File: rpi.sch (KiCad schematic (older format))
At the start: 8 parts, among them J1 Power Connector, P1 RPi-Header

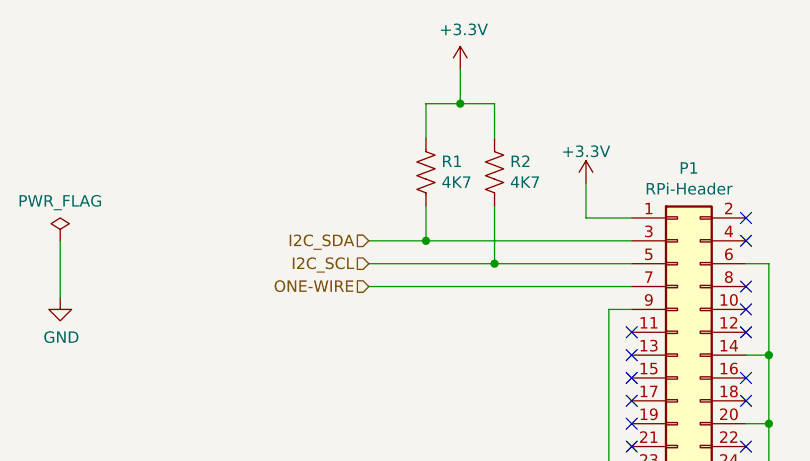
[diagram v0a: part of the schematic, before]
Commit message: Added MFN, MPN, VN and VPN fields for all symbols
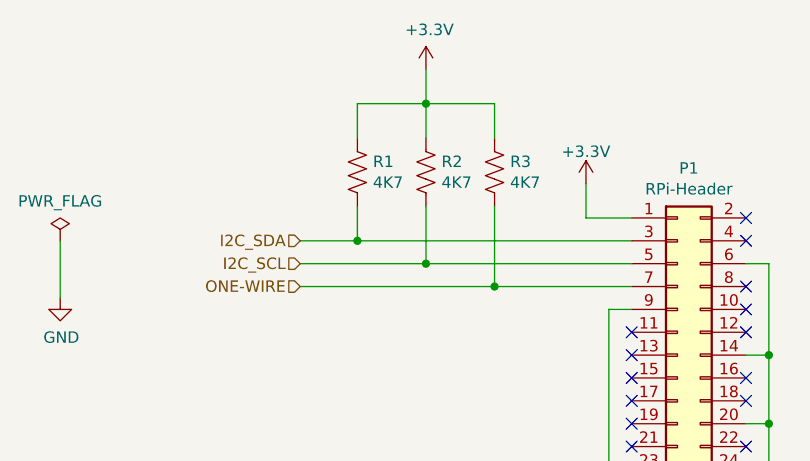
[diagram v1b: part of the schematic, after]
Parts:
- added R3: 4K7, Resistor_SMD:R_0603_1608Metric_Pad1.05x0.95mm_HandSolder, symbol Device:R_US
- J1: MFN (none) -> CUI Devices; MPN (none) -> TBP02R1-381-03BE; VN (none) -> Digikey; VPN (none) -> 102-6481-ND
- MK1, MK2, MK3, MK4: MFN (none) -> None; MPN (none) -> None; VN (none) -> None; VPN (none) -> None
- P1: MFN (none) -> Adafruit Industries LLC; MPN (none) -> 1979; VN (none) -> Digikey; VPN (none) -> 1528-1783-ND
- R1, R2: MFN (none) -> Generic; MPN (none) -> Generic; VN (none) -> Digikey; VPN (none) -> P4.7KDBCT-ND
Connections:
- net +3V3: now also R3.1
- net ONE-WIRE: now also R3.2
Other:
- moved on the sheet: R1, R2
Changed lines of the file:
@@
 F 1 "M2.5" H 6900 5355 50  0000 L CNN
 F 2 "MountingHole:MountingHole_2.7mm_M2.5" H 6800 5400 60  0001 C CNN
-F 3 "" H 6800 5400 60  0001 C CNN
+F 3 "~" H 6800 5400 60  0001 C CNN
+F 4 "None" H 6800 5400 50  0001 C CNN "VN"
+F 5 "None" H 6800 5400 50  0001 C CNN "MFN"
+F 6 "None" H 6800 5400 50  0001 C CNN "MPN"
+F 7 "None" H 6800 5400 50  0001 C CNN "VPN"
 	1    6800 5400
 	1    0    0    -1
@@
 F 1 "M2.5" H 7900 5355 50  0000 L CNN
 F 2 "MountingHole:MountingHole_2.7mm_M2.5" H 7800 5400 60  0001 C CNN
-F 3 "" H 7800 5400 60  0001 C CNN
+F 3 "~" H 7800 5400 60  0001 C CNN
+F 4 "None" H 7800 5400 50  0001 C CNN "VN"
+F 5 "None" H 7800 5400 50  0001 C CNN "MFN"
+F 6 "None" H 7800 5400 50  0001 C CNN "MPN"
+F 7 "None" H 7800 5400 50  0001 C CNN "VPN"
 	1    7800 5400
 	1    0    0    -1
@@
 F 1 "M2.5" H 7400 5355 50  0000 L CNN
 F 2 "MountingHole:MountingHole_2.7mm_M2.5" H 7300 5400 60  0001 C CNN
-F 3 "" H 7300 5400 60  0001 C CNN
+F 3 "~" H 7300 5400 60  0001 C CNN
+F 4 "None" H 7300 5400 50  0001 C CNN "VN"
+F 5 "None" H 7300 5400 50  0001 C CNN "MFN"
+F 6 "None" H 7300 5400 50  0001 C CNN "MPN"
+F 7 "None" H 7300 5400 50  0001 C CNN "VPN"
 	1    7300 5400
 	1    0    0    -1
@@
 F 1 "M2.5" H 8400 5355 50  0000 L CNN
 F 2 "MountingHole:MountingHole_2.7mm_M2.5" H 8300 5400 60  0001 C CNN
-F 3 "" H 8300 5400 60  0001 C CNN
+F 3 "~" H 8300 5400 60  0001 C CNN
+F 4 "None" H 8300 5400 50  0001 C CNN "VN"
+F 5 "None" H 8300 5400 50  0001 C CNN "MFN"
+F 6 "None" H 8300 5400 50  0001 C CNN "MPN"
+F 7 "None" H 8300 5400 50  0001 C CNN "VPN"
 	1    8300 5400
 	1    0    0    -1
@@
 Wire Wire Line
 	7950 3050 7850 3050
-Wire Wire Line
-	6200 3150 7350 3150
-Wire Wire Line
-	6200 3050 6750 3050
-Wire Wire Line
-	7350 2950 6450 2950
 Connection ~ 7250 4050
 Wire Wire Line
@@
 F 1 "RPi-Header" H 7600 4776 50  0000 C CNN
 F 2 "Connector_PinSocket_2.54mm:PinSocket_2x20_P2.54mm_Vertical" H 2700 2800 50  0001 C CNN
-F 3 "" H 2700 2800 50  0001 C CNN
+F 3 "https://media.digikey.com/pdf/Data%20Sheets/Adafruit%20PDFs/1979_Web.pdf" H 2700 2800 50  0001 C CNN
+F 4 "Adafruit Industries LLC" H 7550 3750 50  0001 C CNN "MFN"
+F 5 "1979" H 7550 3750 50  0001 C CNN "MPN"
+F 6 "Digikey" H 7550 3750 50  0001 C CNN "VN"
+F 7 "1528-1783-ND" H 7550 3750 50  0001 C CNN "VPN"
 	1    7550 3750
 	1    0    0    -1
@@
 NoConn ~ 7350 3650
 NoConn ~ 7350 4250
-Text HLabel 6200 2950 0    50   Input ~ 0
+Text HLabel 5900 2950 0    50   Input ~ 0
 I2C_SDA
-Text HLabel 6200 3050 0    50   Input ~ 0
+Text HLabel 5900 3050 0    50   Input ~ 0
 I2C_SCL
-Text HLabel 6200 3150 0    50   Input ~ 0
+Text HLabel 5900 3150 0    50   Input ~ 0
 ONE-WIRE
 $Comp
@@
 F 1 "Power Connector" H 3768 3766 50  0000 C CNN
 F 2 "Connector_Phoenix_MC:PhoenixContact_MC_1,5_3-G-3.81_1x03_P3.81mm_Horizontal" H 3850 4000 50  0001 C CNN
-F 3 "~" H 3850 4000 50  0001 C CNN
+F 3 "https://www.cuidevices.com/product/resource/tbp02r1-381.pdf" H 3850 4000 50  0001 C CNN
+F 4 "Digikey" H 3850 4000 50  0001 C CNN "VN"
+F 5 "CUI Devices" H 3850 4000 50  0001 C CNN "MFN"
+F 6 "TBP02R1-381-03BE" H 3850 4000 50  0001 C CNN "MPN"
+F 7 "102-6481-ND" H 3850 4000 50  0001 C CNN "VPN"
 	1    3850 4000
 	-1   0    0    1
@@
 L Device:R_US R?
 U 1 1 5E5D64A6
-P 6450 2650
+P 6150 2650
 AR Path="/5E5D64A6" Ref="R?"  Part="1"
 AR Path="/5E624F1D/5E5D64A6" Ref="R?"  Part="1"
 AR Path="/5E49EFD8/5E5D64A6" Ref="R1"  Part="1"
-F 0 "R1" H 6518 2696 50  0000 L CNN
+F 0 "R1" H 6218 2696 50  0000 L CNN
+F 1 "4K7" H 6218 2605 50  0000 L CNN
+F 2 "Resistor_SMD:R_0603_1608Metric_Pad1.05x0.95mm_HandSolder" V 6190 2640 50  0001 C CNN
+F 3 "~" H 6150 2650 50  0001 C CNN
+F 4 "Digikey" H 6150 2650 50  0001 C CNN "VN"
+F 5 "Generic" H 6150 2650 50  0001 C CNN "MFN"
+F 6 "Generic" H 6150 2650 50  0001 C CNN "MPN"
+F 7 "P4.7KDBCT-ND" H 6150 2650 50  0001 C CNN "VPN"
+	1    6150 2650
+	1    0    0    -1
+$EndComp
+$Comp
+L power:+3.3V #PWR?
+U 1 1 5E5D64AD
+P 6450 2200
+AR Path="/5E5D64AD" Ref="#PWR?"  Part="1"
+AR Path="/5E624F1D/5E5D64AD" Ref="#PWR?"  Part="1"
+AR Path="/5E49EFD8/5E5D64AD" Ref="#PWR0139"  Part="1"
+F 0 "#PWR0139" H 6450 2050 50  0001 C CNN
+F 1 "+3.3V" H 6465 2373 50  0000 C CNN
+F 2 "" H 6450 2200 50  0001 C CNN
+F 3 "" H 6450 2200 50  0001 C CNN
+	1    6450 2200
+	1    0    0    -1
+$EndComp
+Wire Wire Line
+	6750 2350 6750 2500
+$Comp
+L Device:R_US R?
+U 1 1 5E5D64B5
+P 6450 2650
+AR Path="/5E5D64B5" Ref="R?"  Part="1"
+AR Path="/5E624F1D/5E5D64B5" Ref="R?"  Part="1"
+AR Path="/5E49EFD8/5E5D64B5" Ref="R2"  Part="1"
+F 0 "R2" H 6518 2696 50  0000 L CNN
 F 1 "4K7" H 6518 2605 50  0000 L CNN
 F 2 "Resistor_SMD:R_0603_1608Metric_Pad1.05x0.95mm_HandSolder" V 6490 2640 50  0001 C CNN
 F 3 "~" H 6450 2650 50  0001 C CNN
+F 4 "Digikey" H 6450 2650 50  0001 C CNN "VN"
+F 5 "Generic" H 6450 2650 50  0001 C CNN "MFN"
+F 6 "Generic" H 6450 2650 50  0001 C CNN "MPN"
+F 7 "P4.7KDBCT-ND" H 6450 2650 50  0001 C CNN "VPN"
 	1    6450 2650
 	1    0    0    -1
 $EndComp
-$Comp
-L power:+3.3V #PWR?
-U 1 1 5E5D64AD
-P 6600 2200
-AR Path="/5E5D64AD" Ref="#PWR?"  Part="1"
-AR Path="/5E624F1D/5E5D64AD" Ref="#PWR?"  Part="1"
-AR Path="/5E49EFD8/5E5D64AD" Ref="#PWR0139"  Part="1"
-F 0 "#PWR0139" H 6600 2050 50  0001 C CNN
-F 1 "+3.3V" H 6615 2373 50  0000 C CNN
-F 2 "" H 6600 2200 50  0001 C CNN
-F 3 "" H 6600 2200 50  0001 C CNN
-	1    6600 2200
-	1    0    0    -1
-$EndComp
-Wire Wire Line
-	6750 2350 6750 2500
-$Comp
-L Device:R_US R?
-U 1 1 5E5D64B5
-P 6750 2650
-AR Path="/5E5D64B5" Ref="R?"  Part="1"
-AR Path="/5E624F1D/5E5D64B5" Ref="R?"  Part="1"
-AR Path="/5E49EFD8/5E5D64B5" Ref="R2"  Part="1"
-F 0 "R2" H 6818 2696 50  0000 L CNN
-F 1 "4K7" H 6818 2605 50  0000 L CNN
-F 2 "Resistor_SMD:R_0603_1608Metric_Pad1.05x0.95mm_HandSolder" V 6790 2640 50  0001 C CNN
-F 3 "~" H 6750 2650 50  0001 C CNN
-	1    6750 2650
-	1    0    0    -1
-$EndComp
-Wire Wire Line
-	6450 2350 6600 2350
-Wire Wire Line
-	6600 2200 6600 2350
-Connection ~ 6600 2350
-Wire Wire Line
-	6600 2350 6750 2350
+Wire Wire Line
+	6450 2200 6450 2350
 Wire Wire Line
 	6450 2500 6450 2350
 Wire Wire Line
-	6450 2800 6450 2950
-Connection ~ 6450 2950
-Wire Wire Line
-	6450 2950 6200 2950
-Wire Wire Line
-	6750 2800 6750 3050
-Connection ~ 6750 3050
-Wire Wire Line
-	6750 3050 7350 3050
+	6150 2950 5900 2950
 NoConn ~ 7850 3150
 NoConn ~ 7850 3250
@@
 Wire Wire Line
 	4850 2950 4850 3200
+$Comp
+L Device:R_US R?
+U 1 1 5E62CDA9
+P 6750 2650
+AR Path="/5E62CDA9" Ref="R?"  Part="1"
+AR Path="/5E64C909/5E62CDA9" Ref="R?"  Part="1"
+AR Path="/5E49EFD8/5E62CDA9" Ref="R3"  Part="1"
+F 0 "R3" H 6818 2696 50  0000 L CNN
+F 1 "4K7" H 6818 2605 50  0000 L CNN
+F 2 "Resistor_SMD:R_0603_1608Metric_Pad1.05x0.95mm_HandSolder" V 6790 2640 50  0001 C CNN
+F 3 "~" H 6750 2650 50  0001 C CNN
+F 4 "Digikey" H 6750 2650 50  0001 C CNN "VN"
+F 5 "Generic" H 6750 2650 50  0001 C CNN "MFN"
+F 6 "Generic" H 6750 2650 50  0001 C CNN "MPN"
+F 7 "P4.7KDBCT-ND" H 6750 2650 50  0001 C CNN "VPN"
+	1    6750 2650
+	1    0    0    -1
+$EndComp
+Wire Wire Line
+	6150 2350 6150 2500
+Wire Wire Line
+	6150 2350 6450 2350
+Connection ~ 6450 2350
+Wire Wire Line
+	6450 2350 6750 2350
+Wire Wire Line
+	6150 2800 6150 2950
+Wire Wire Line
+	6150 2950 7350 2950
+Connection ~ 6150 2950
+Wire Wire Line
+	5900 3050 6450 3050
+Wire Wire Line
+	5900 3150 6750 3150
+Wire Wire Line
+	6450 2800 6450 3050
+Connection ~ 6450 3050
+Wire Wire Line
+	6450 3050 7350 3050
+Wire Wire Line
+	6750 2800 6750 3150
+Connection ~ 6750 3150
+Wire Wire Line
+	6750 3150 7350 3150
 $EndSCHEMATC
